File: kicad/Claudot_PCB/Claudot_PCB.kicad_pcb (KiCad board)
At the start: 2 copper layers, 104.8 x 57.2 mm, 58 parts, among them J1 Conn_01x04, SW1 SW_Push, SW10 SW_Push, SW11 SW_Push, SW12 RotaryEncoder, SW2 SW_Push, SW3 SW_Push, SW4 SW_Push, SW5 SW_Push, SW6 SW_Push, SW7 SW_Push, SW8 SW_Push, SW9 SW_Push, U1 RP2040, U2 W25Q16JVUXIQ, U3 AP2112K-3.3, Y1 12MHz

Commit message: Update schematic and pcb
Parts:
- moved R4 2.94 mm to (108.6, 92.2)
- moved R3 2.94 mm to (108.6, 91.2), turned to 0 degrees
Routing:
- net GND: vias 19 -> 21
- net +3V3: vias 4 -> 5
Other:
- board text added: "B"
- board text added: "R"
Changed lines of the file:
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@@
 			(unlocked yes)
 			(layer "F.SilkS")
+			(hide yes)
 			(effects
 				(font
@@
 	(footprint "Resistor_SMD:R_0402_1005Metric"
 		(layer "F.Cu")
-		(at 109.21 89.3)
+		(at 108.60875 92.175)
 		(descr "Resistor SMD 0402 (1005 Metric), square (rectangular) end terminal, IPC-7351 nominal, (Body size source: IPC-SM-782 page 72, https://www.pcb-3d.com/wordpress/wp-content/uploads/ipc-sm-782a_amendment_1_and_2.pdf), generated with kicad-footprint-generator")
 		(tags "resistor")
@@
 	(footprint "Resistor_SMD:R_0402_1005Metric"
 		(layer "F.Cu")
-		(at 109.2 88.3 180)
+		(at 108.60875 91.175)
 		(descr "Resistor SMD 0402 (1005 Metric), square (rectangular) end terminal, IPC-7351 nominal, (Body size source: IPC-SM-782 page 72, https://www.pcb-3d.com/wordpress/wp-content/uploads/ipc-sm-782a_amendment_1_and_2.pdf), generated with kicad-footprint-generator")
 		(tags "resistor")
@@
 		)
 		(property "LCSC" "C25744"
-			(at 0 0 180)
+			(at 0 0 0)
 			(unlocked yes)
 			(layer "F.Fab")
@@
 		(attr smd)
 		(fp_line
-			(start -0.153641 0.38)
-			(end 0.153641 0.38)
+			(start -0.153641 -0.38)
+			(end 0.153641 -0.38)
 			(stroke
 				(width 0.12)
@@
 		)
 		(fp_line
-			(start -0.153641 -0.38)
-			(end 0.153641 -0.38)
+			(start -0.153641 0.38)
+			(end 0.153641 0.38)
 			(stroke
 				(width 0.12)
@@
 		)
 		(fp_line
-			(start 0.93 0.47)
-			(end -0.93 0.47)
+			(start -0.93 -0.47)
+			(end 0.93 -0.47)
 			(stroke
 				(width 0.05)
@@
 		)
 		(fp_line
-			(start 0.93 -0.47)
-			(end 0.93 0.47)
+			(start -0.93 0.47)
+			(end -0.93 -0.47)
 			(stroke
 				(width 0.05)
@@
 		)
 		(fp_line
-			(start -0.93 0.47)
-			(end -0.93 -0.47)
+			(start 0.93 -0.47)
+			(end 0.93 0.47)
 			(stroke
 				(width 0.05)
@@
 		)
 		(fp_line
-			(start -0.93 -0.47)
-			(end 0.93 -0.47)
+			(start 0.93 0.47)
+			(end -0.93 0.47)
 			(stroke
 				(width 0.05)
@@
 		)
 		(fp_line
-			(start 0.525 0.27)
-			(end -0.525 0.27)
+			(start -0.525 -0.27)
+			(end 0.525 -0.27)
 			(stroke
 				(width 0.1)
@@
 		)
 		(fp_line
-			(start 0.525 -0.27)
-			(end 0.525 0.27)
+			(start -0.525 0.27)
+			(end -0.525 -0.27)
 			(stroke
 				(width 0.1)
@@
 		)
 		(fp_line
-			(start -0.525 0.27)
-			(end -0.525 -0.27)
+			(start 0.525 -0.27)
+			(end 0.525 0.27)
 			(stroke
 				(width 0.1)
@@
 		)
 		(fp_line
-			(start -0.525 -0.27)
-			(end 0.525 -0.27)
+			(start 0.525 0.27)
+			(end -0.525 0.27)
 			(stroke
 				(width 0.1)
@@
 		)
 		(pad "1" smd roundrect
-			(at -0.51 0 180)
+			(at -0.51 0)
 			(size 0.54 0.64)
 			(layers "F.Cu" "F.Mask" "F.Paste")
@@
 		)
 		(pad "2" smd roundrect
-			(at 0.51 0 180)
+			(at 0.51 0)
 			(size 0.54 0.64)
 			(layers "F.Cu" "F.Mask" "F.Paste")
@@
 			(unlocked yes)
 			(layer "F.SilkS")
+			(hide yes)
 			(effects
 				(font
@@
 	)
 	(gr_line
+		(start 106.84375 94.325)
+		(end 107.868749 94.325)
+		(stroke
+			(width 0.2)
+			(type solid)
+		)
+		(layer "F.Cu")
+		(net 46)
+	)
+	(gr_line
 		(start 119.6625 98.6875)
 		(end 119.6625 99.425)
@@
 	)
 	(gr_line
+		(start 106.84375 98.325)
+		(end 107.868749 98.325)
+		(stroke
+			(width 0.2)
+			(type solid)
+		)
+		(layer "F.Cu")
+		(net 46)
+	)
+	(gr_line
 		(start 114.8875 92.45)
 		(end 115.0875 92.65)
@@
 	)
 	(gr_line
+		(start 108.09875 91.175)
+		(end 108.09875 90.355)
+		(stroke
+			(width 0.2)
+			(type solid)
+		)
+		(layer "F.Cu")
+		(net 67)
+	)
+	(gr_line
 		(start 118.8625 90.275)
 		(end 118.8625 91.8125)
@@
 	)
 	(gr_line
+		(start 109.11875 91.175)
+		(end 109.11875 92.175)
+		(stroke
+			(width 0.2)
+			(type solid)
+		)
+		(layer "F.Cu")
+		(net 88)
+	)
+	(gr_line
 		(start 122.0625 89.525)
 		(end 122.0625 88.775)
@@
 	)
 	(gr_line
+		(start 106.84375 92.175)
+		(end 108.09875 92.175)
+		(stroke
+			(width 0.2)
+			(type solid)
+		)
+		(layer "F.Cu")
+		(net 89)
+	)
+	(gr_line
 		(start 113.7375 85.05)
 		(end 113.3375 84.65)
@@
 		(layer "F.Fab")
 	)
+	(gr_text "R"
+		(at 106.937 97.88 0)
+		(layer "F.SilkS")
+		(effects
+			(font
+				(size 1 1)
+				(thickness 0.153)
+			)
+			(justify left bottom)
+		)
+	)
+	(gr_text "B"
+		(at 106.937 93.29 0)
+		(layer "F.SilkS")
+		(effects
+			(font
+				(size 1 1)
+				(thickness 0.153)
+			)
+			(justify left)
+		)
+	)
 	(segment
 		(start 118.0625 98.6875)
@@
 	)
 	(via
+		(at 107.868749 94.325)
+		(size 0.6)
+		(drill 0.3)
+		(layers "F.Cu" "B.Cu")
+		(remove_unused_layers yes)
+		(keep_end_layers yes)
+		(zone_layer_connections)
+		(net 46)
+	)
+	(via
 		(at 111.9125 90.35)
 		(size 0.6)
@@
 	)
 	(via
+		(at 107.868749 98.325)
+		(size 0.6)
+		(drill 0.3)
+		(layers "F.Cu" "B.Cu")
+		(remove_unused_layers yes)
+		(keep_end_layers yes)
+		(zone_layer_connections)
+		(net 46)
+	)
+	(via
 		(at 117.6625 102.025)
 		(size 0.6)
@@
 		(size 0.6)
 		(drill 0.3)
+		(layers "F.Cu" "B.Cu")
+		(net 67)
+	)
+	(via
+		(at 108.09875 90.355)
+		(size 0.6)
+		(drill 0.3)

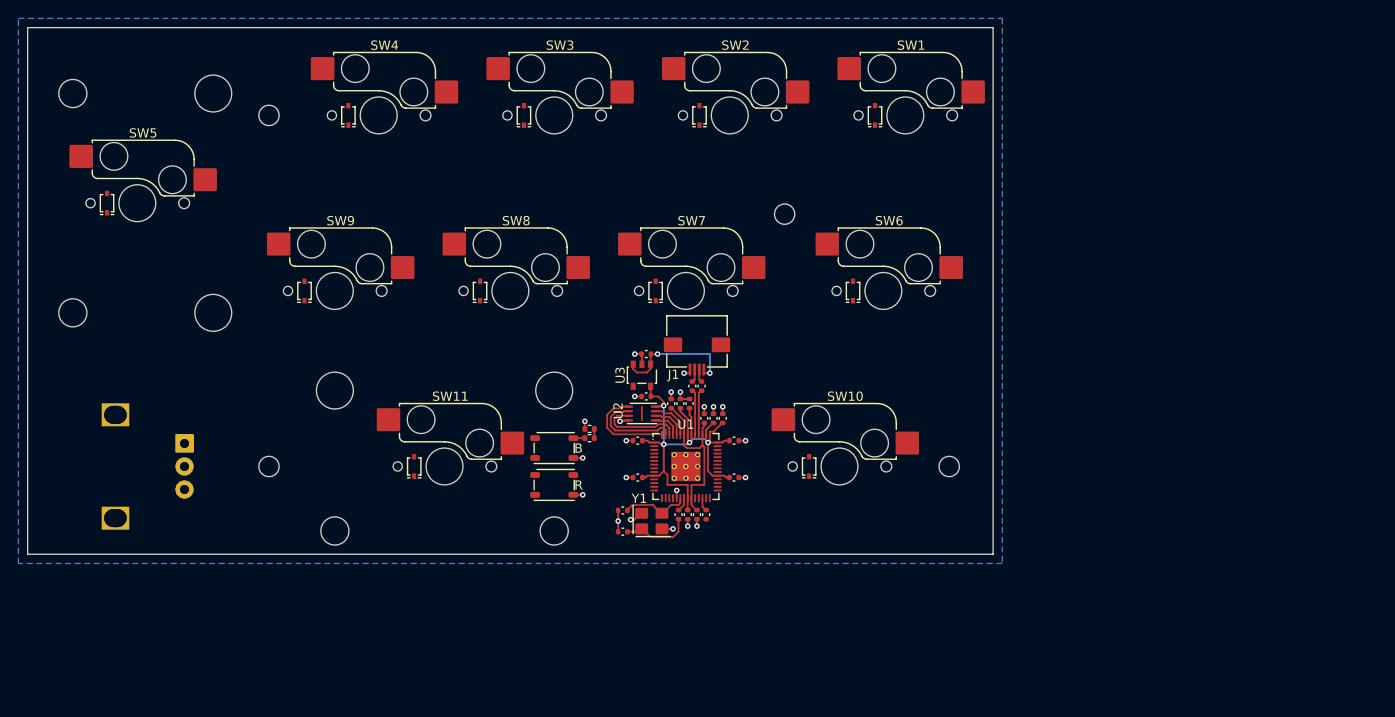
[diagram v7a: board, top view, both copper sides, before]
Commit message: Add USB-C connector
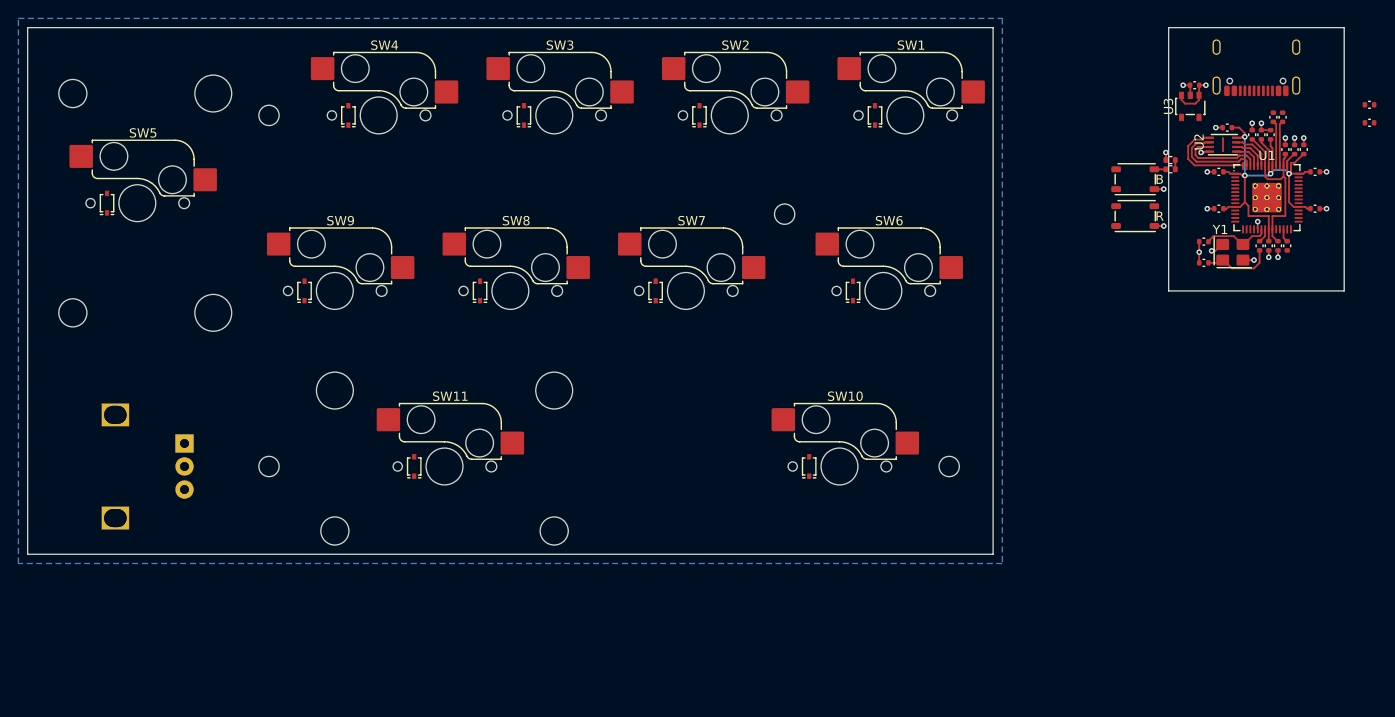
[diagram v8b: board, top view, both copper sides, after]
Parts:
- added R7: 5.1K, Library:R_0402, F.Cu at (193.2, 58.0)
- added R8: 5.1K, Library:R_0402, F.Cu at (193.2, 56.0)
- J1: value Conn_01x04 -> TYPE-C-31-M-12; footprint Library:AFC01-S04FCC-00 -> Library:TYPE-C-31-M-12
- moved C1 69.5 mm to (175.3, 70.8)
- moved C10 69.5 mm to (186.1, 60.9)
- moved C11 69.5 mm to (182.5, 59.2)
- moved C12 69.5 mm to (181.5, 59.2)
- moved C14 69.5 mm to (180.5, 59.2)
- moved C2 69.5 mm to (175.3, 73.2)
- moved C3 69.5 mm to (185.1, 60.9)
- moved C4 69.5 mm to (184.1, 60.9)
- moved C5 69.5 mm to (176.9, 63.3)
- moved C6 69.5 mm to (176.9, 67.3)
- moved C8 69.5 mm to (187.3, 67.3)
- moved C9 69.5 mm to (187.3, 63.3)
- moved U1 69.5 mm to (182.1, 66.1)
- moved U2 69.5 mm to (177.3, 60.3)
- moved C13 69.5 mm to (183.3, 71.3)
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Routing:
- net GND: vias 21 -> 20
- net +5V: vias 2 -> 1
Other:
- board size 104.8 x 57.2 mm -> 142.9 x 57.2 mm
